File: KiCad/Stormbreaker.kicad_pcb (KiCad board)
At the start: 4 copper layers, 50.2 x 21 mm, 45 parts, among them J1 Micro_SD_Card_Det2, J2 USB_C_Receptacle_USB2.0_14P, J3 Conn_01x03, J4 FAN, J5 Conn_01x02, Q1 PMOS, Q2 NMOS, SW1 SW_Push, U1 BQ25895RTW, U3 ATtiny1616-M

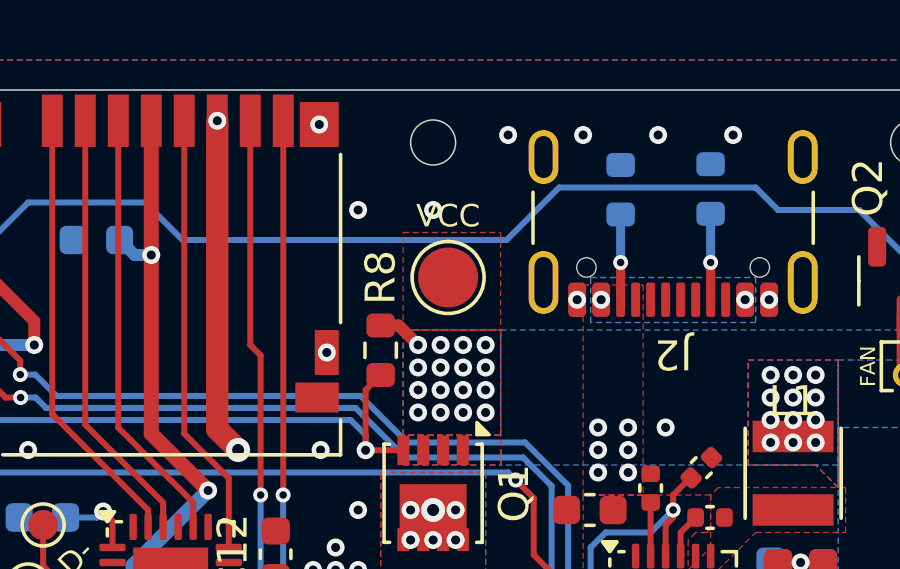
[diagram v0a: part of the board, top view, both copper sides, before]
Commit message: Adjust position of power pad
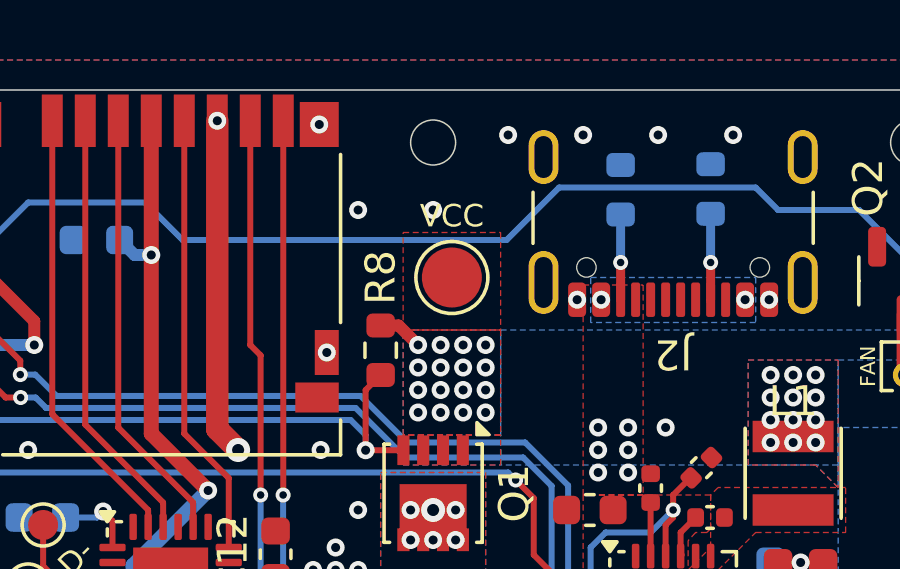
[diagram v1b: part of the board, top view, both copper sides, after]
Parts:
- moved TP8 0.12 mm to (140.6, 47.2)
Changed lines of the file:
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@@
 	(footprint "TestPoint:TestPoint_Pad_D2.0mm"
 		(layer "F.Cu")
-		(at 140.5 47.25 180)
+		(at 140.625 47.25 180)
 		(descr "SMD pad as test Point, diameter 2.0mm")
 		(tags "test point SMD pad")

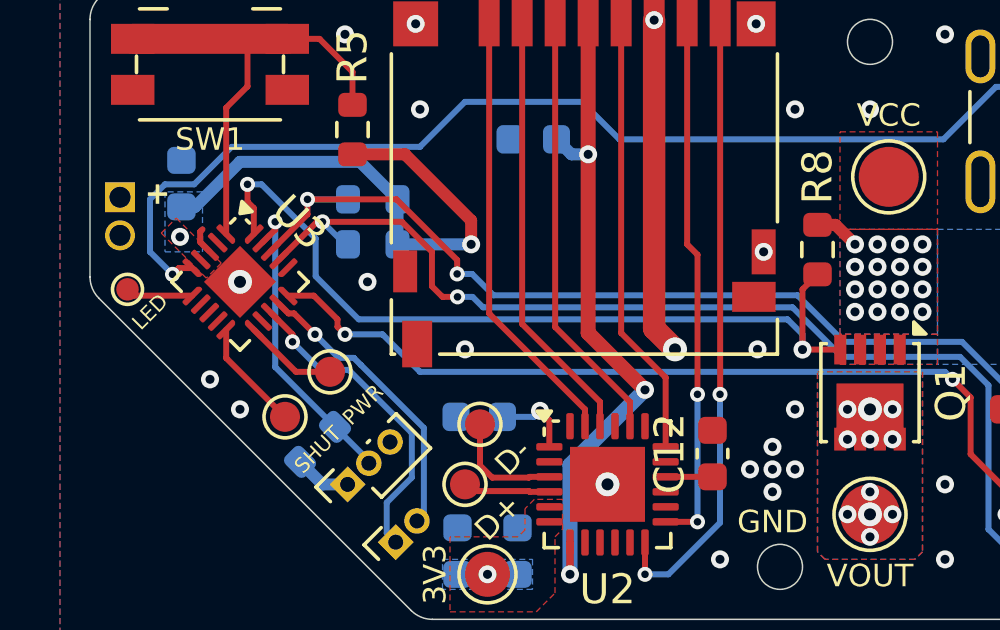
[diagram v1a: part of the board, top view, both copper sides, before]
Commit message: Begin interface code, implement safety features
Now loads (and writes) various settings from (and to) EEPROM. Added error handling, to an extent. Added comments for easier understanding. Emergency power-off and shipping mode in over-temp situations. Added ALERT pin for over-temp situations to PCB.
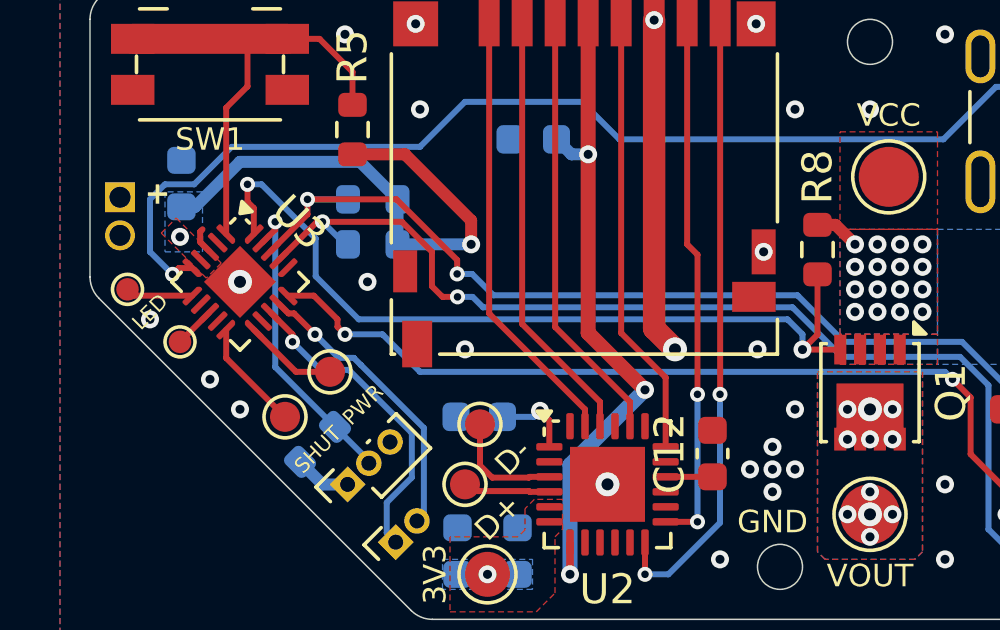
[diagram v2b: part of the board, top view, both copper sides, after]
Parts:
- added TP11: ALERT, TestPoint:TestPoint_Pad_D1.0mm, F.Cu at (117.0, 52.8)
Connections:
- U3 pad 8: unconnected-(U3-PA7-Pad8) -> /ALERT
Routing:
- net /ALERT: track 0.00 -> 1.38 mm
- net GND: vias 34 -> 35
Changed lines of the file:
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@@
 	(net 36 "unconnected-(U1-~{QON}-Pad12)")
 	(net 37 "unconnected-(U3-PB5-Pad9)")
-	(net 38 "unconnected-(U3-PA7-Pad8)")
+	(net 38 "/ALERT")
 	(net 39 "/PA0")
 	(net 40 "unconnected-(U3-PC1-Pad16)")
@@
 			(layers "F.Cu" "F.Mask" "F.Paste")
 			(roundrect_rratio 0.25)
-			(net 38 "unconnected-(U3-PA7-Pad8)")
+			(net 38 "/ALERT")
 			(pinfunction "PA7")
 			(pintype "bidirectional")
@@
 		)
 	)
+	(footprint "TestPoint:TestPoint_Pad_D1.0mm"
+		(layer "F.Cu")
+		(at 117 52.75)
+		(descr "SMD pad as test Point, diameter 1.0mm")
+		(tags "test point SMD pad")
+		(property "Reference" "TP11"
+			(at 0 -1.448 0)
+			(layer "F.Fab")
+			(hide yes)
+			(effects
+				(font
+					(size 1 1)
+					(thickness 0.15)
+				)
+			)
+		)
+		(property "Value" "ALERT"
+			(at 0 1.55 0)
+			(layer "F.Fab")
+			(hide yes)
+			(effects
+				(font
+					(size 1 1)
+					(thickness 0.15)
+				)
+			)
+		)
+		(property "Datasheet" ""
+			(at 0 0 0)
+			(layer "F.Fab")
+			(hide yes)
+			(effects
+				(font
+					(size 1.27 1.27)
+					(thickness 0.15)
+				)
+			)
+		)
+		(property "Description" "test point"
+			(at 0 0 0)
+			(layer "F.Fab")
+			(hide yes)
+			(effects
+				(font
+					(size 1.27 1.27)
+					(thickness 0.15)
+				)
+			)
+		)
+		(property ki_fp_filters "Pin* Test*")
+		(sheetname "/")
+		(sheetfile "Stormbreaker.kicad_sch")
+		(attr exclude_from_pos_files)
+		(fp_circle
+			(center 0 0)
+			(end 0 0.5)
+			(stroke
+				(width 0.12)
+				(type solid)
+			)
+			(fill no)
+			(layer "F.SilkS")
+		)
+		(fp_circle
+			(center 0 0)
+			(end 0.75 0)
+			(stroke
+				(width 0.05)
+				(type solid)
+			)
+			(fill no)
+			(layer "F.CrtYd")
+		)
+		(pad "1" smd circle
+			(at 0 0)
+			(size 0.75 0.75)
+			(layers "F.Cu" "F.Mask")
+			(net 38 "/ALERT")
+			(pinfunction "1")
+			(pintype "passive")
+		)
+		(embedded_fonts no)
+	)
 	(footprint "Package_DFN_QFN:HVQFN-24-1EP_4x4mm_P0.5mm_EP2.5x2.5mm"
 		(layer "F.Cu")
@@
 	)
 	(via
+		(at 116 52)
+		(size 0.6)
+		(drill 0.3)
+		(layers "F.Cu" "B.Cu")
+		(free yes)
+		(net 1)
+	)
+	(via
 		(at 119 55)
 		(size 0.6)
@@
 	)
 	(segment
+		(start 117 52.75)
+		(end 117.974695 51.775305)
+		(width 0.2)
+		(layer "F.Cu")
+		(net 38)
+	)
+	(segment
 		(start 120.174126 48.75)
 		(end 120.174126 49.010188)
@@
 	)
 	(segment
-		(start 137.75 51)
+		(start 138.25 52.5075)
 		(end 137.75 53.0075)
 		(width 0.2)
@@
 	)
 	(segment
+		(start 138.25 50.5)
+		(end 138.25 52.5075)
+		(width 0.2)
+		(layer "F.Cu")
+		(net 50)
+	)
+	(segment
 		(start 119.25 48.080762)
 		(end 119.459619 48.290381)
@@
 		(width 0.2)
 		(layer "F.Cu")
-		(net 50)
-	)
-	(segment
-		(start 138.25 50.5)
-		(end 137.75 51)
-		(width 0.2)
-		(layer "F.Cu")

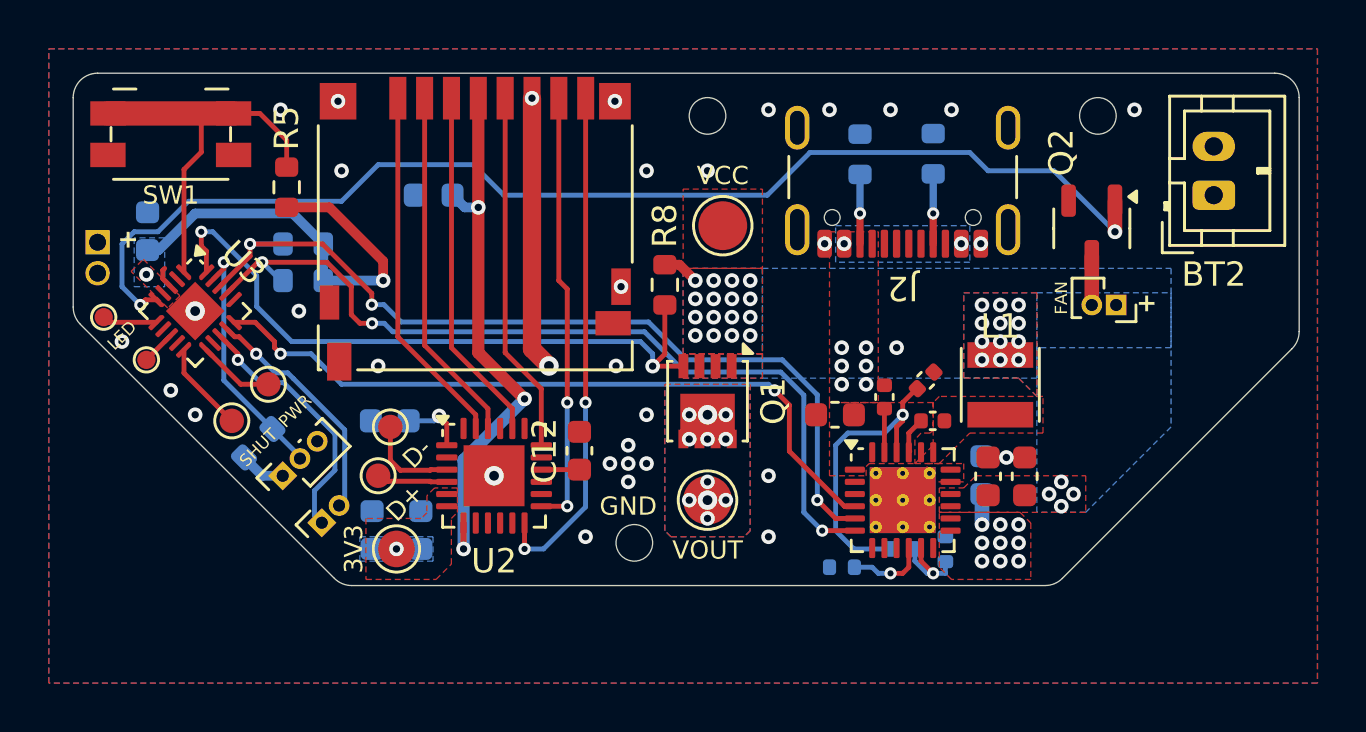
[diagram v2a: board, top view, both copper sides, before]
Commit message: Modify fan pin, implement fan control, misc
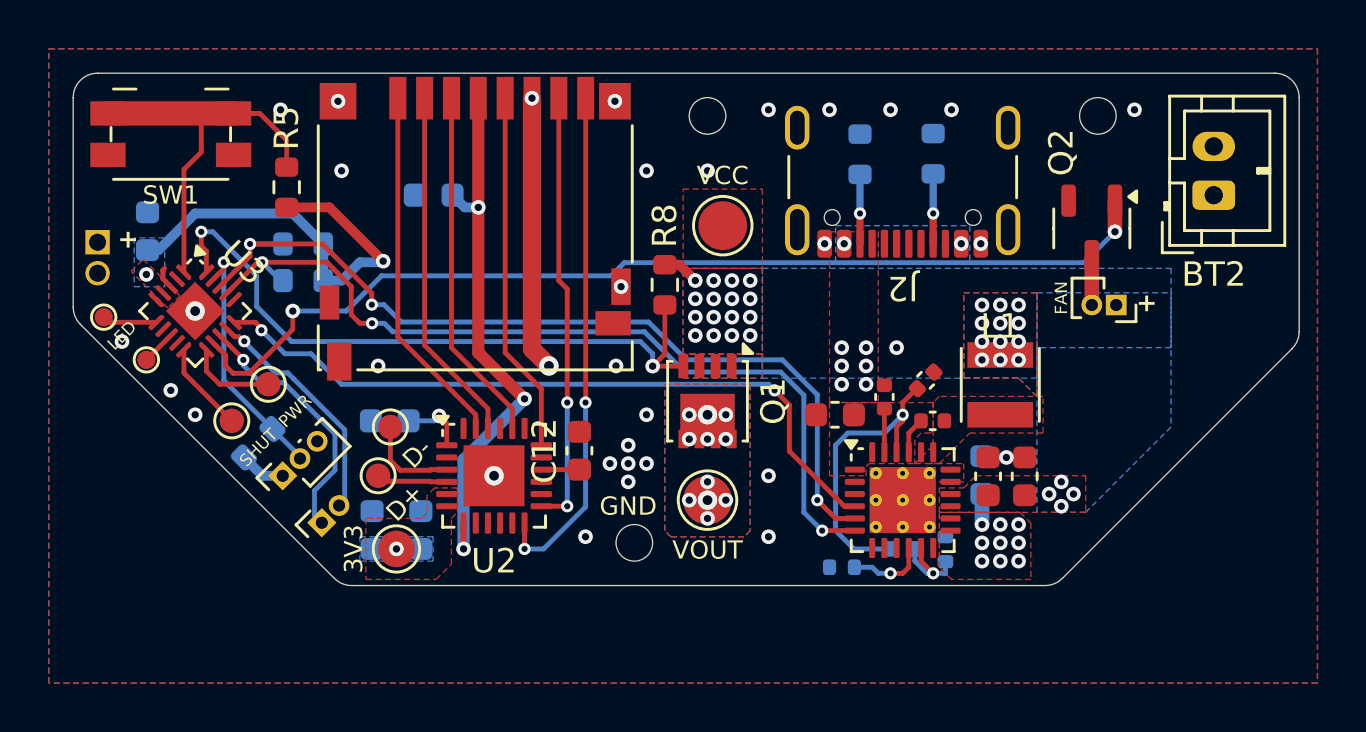
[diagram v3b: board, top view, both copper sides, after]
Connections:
- Q2 pad 1: Net-(Q2-G) -> FAN_PWM
- U3 pad 12: unconnected-(U3-PB2-Pad12) -> FAN_PWM
- U3 pad 5: Net-(Q2-G) -> unconnected-(U3-PA4-Pad5)
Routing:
- net Net-(Q2-G): track 49.5 -> 0.00 mm, vias 2 -> 0
- net FAN_PWM: track 0.00 -> 41.8 mm, vias 0 -> 2
- net /Wii_POWER: track 3.12 -> 3.63 mm
- net GND: vias 35 -> 34

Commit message: Misc minor PCB modifications
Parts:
- moved TP2 0.35 mm to (126.8, 55.8)
- moved TP6 0.35 mm to (122.2, 54.0)
- moved TP7 0.35 mm to (120.8, 55.5)
- moved TP1 0.25 mm to (126.5, 57.8)
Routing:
- net VCC: track 20.9 -> 23.8 mm
- net GND: track 12.1 -> 11.3 mm, vias 34 -> 32
- net Net-(Q1-G): track 27.5 -> 26.7 mm
- net D-: track 3.86 -> 3.18 mm
- net SCL_2: track 35.8 -> 35.2 mm
- net /PA0: track 10.2 -> 10.7 mm

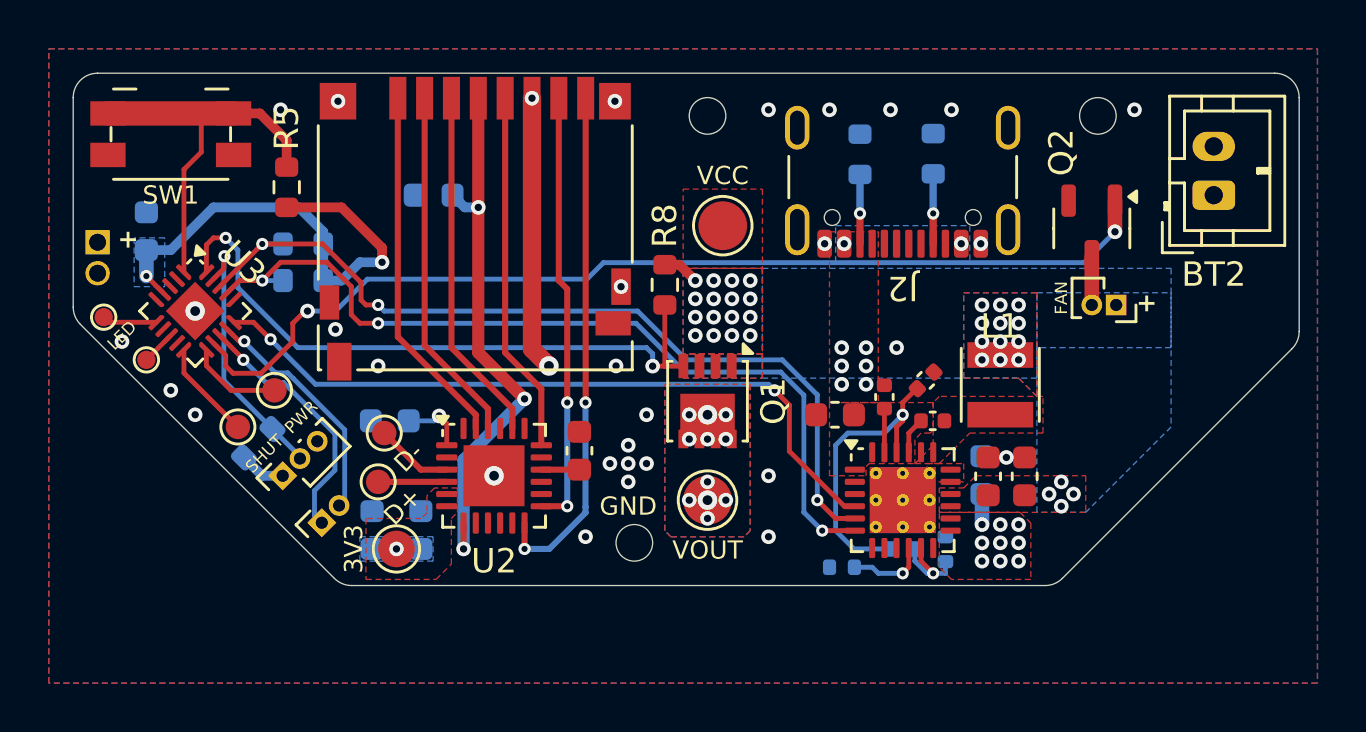
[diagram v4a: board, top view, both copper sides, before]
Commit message: Add USB-C PD circuitry
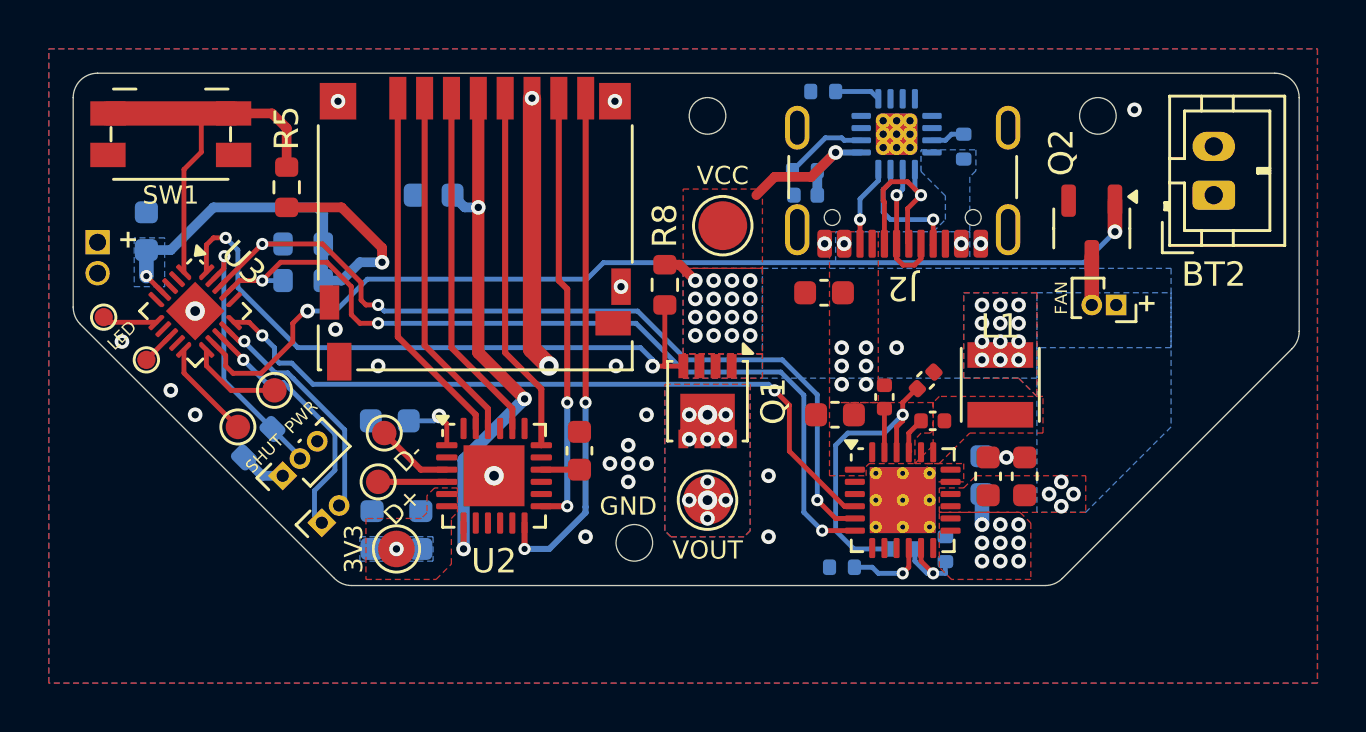
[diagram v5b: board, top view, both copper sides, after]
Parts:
- removed R4: 5.1k, Resistor_SMD:R_0603_1608Metric
- added C14: 10uF, Capacitor_SMD:C_0603_1608Metric, F.Cu at (144.8, 50.0)
- added C15: 1uF, Capacitor_SMD:C_0402_1005Metric, B.Cu at (144.0, 46.0)
- added R11: 10k, Resistor_SMD:R_0402_1005Metric, B.Cu at (150.5, 44.0)
- added R12: 6.04k, Resistor_SMD:R_0402_1005Metric, B.Cu at (144.7, 41.8)
- added U4: HUSB238A, Package_DFN_QFN:QFN-16-1EP_3x3mm_P0.5mm_EP1.7x1.7mm_ThermalVias, B.Cu at (147.8, 43.5)
- R6: value 5.1k -> 900k; footprint Resistor_SMD:R_0603_1608Metric -> Resistor_SMD:R_0402_1005Metric
- moved R6 2.36 mm to (144.0, 45.0), turned to 180 degrees
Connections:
- J2 pad A5: Net-(J2-CC1) -> CC1
- J2 pad A6: unconnected-(J2-D+-PadA6) -> D+_2
- J2 pad A7: unconnected-(J2-D--PadA7) -> D-_2
- J2 pad B5: Net-(J2-CC2) -> CC2
- J2 pad B6: unconnected-(J2-D+-PadB6) -> D+_2
- J2 pad B7: unconnected-(J2-D--PadB7) -> D-_2
- R6 pad 1: GND -> VCC
- R6 pad 2: Net-(J2-CC2) -> Net-(U4-~{DEBUG})
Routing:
- net D+_2: track 0.00 -> 7.54 mm, vias 0 -> 1
- net VCC: track 23.8 -> 31.3 mm, vias 34 -> 35
- net D-_2: track 0.00 -> 5.58 mm, vias 0 -> 1
- net CC1: track 0.00 -> 5.11 mm, vias 0 -> 1
- net Net-(U4-~{DEBUG}): track 0.00 -> 3.42 mm
- net CC2: track 0.00 -> 3.35 mm, vias 0 -> 1
- net Net-(J2-CC1): track 2.94 -> 0.00 mm, vias 1 -> 0
- net Net-(J2-CC2): track 2.84 -> 0.00 mm, vias 1 -> 0
- net Net-(U4-SDA): track 0.00 -> 1.87 mm
- net Net-(U4-GATE): track 0.00 -> 1.40 mm
- net GND: vias 32 -> 27

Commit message: Adjustments to PD chip, WIP
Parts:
- C15: value 1uF -> 1μF
- moved R6 1.43 mm to (145.0, 44.0), turned to 90 degrees
- moved C15 0.56 mm to (144.3, 45.5)
- moved C11 0.50 mm to (128.7, 46.5)
- moved R11 0.30 mm to (150.5, 43.7)
- moved U4 0.30 mm to (147.8, 43.2)
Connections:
- C15 pad 1: VCC -> Net-(U4-VDD)
- J2 pad A6: D+_2 -> unconnected-(J2-D+-PadA6)
- J2 pad A7: D-_2 -> unconnected-(J2-D--PadA7)
- J2 pad B6: D+_2 -> unconnected-(J2-D+-PadB6)
- J2 pad B7: D-_2 -> unconnected-(J2-D--PadB7)
- R6 pad 1: VCC -> VBUS
- U4 pad 1: D+_2 -> unconnected-(U4-D+-Pad1)
- U4 pad 2: D-_2 -> unconnected-(U4-D--Pad2)
- U4 pad 5: VCC -> Net-(U4-VDD)
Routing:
- net D+_2: track 7.54 -> 0.00 mm, vias 1 -> 0
- net VCC: track 31.3 -> 24.2 mm, vias 35 -> 34
- net D-_2: track 5.58 -> 0.00 mm, vias 1 -> 0
- net Net-(U4-VDD): track 0.00 -> 2.78 mm
- net Net-(U4-~{DEBUG}): track 3.42 -> 1.31 mm
- net CC2: track 3.35 -> 3.95 mm
